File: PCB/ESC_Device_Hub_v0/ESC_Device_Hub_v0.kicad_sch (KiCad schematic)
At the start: 137 parts, among them J1 Conn_01x04, J10 Conn_01x06, J11 Conn_01x02, J12 Conn_01x02, J13 Conn_01x02, J14 Conn_01x02, J15 Conn_01x02, J16 Conn_01x02, J17 Conn_01x02, J18 Conn_01x02, J19 Conn_01x05, J2 Conn_01x04, J20 Conn_01x01, J21 Conn_01x01, J22 Conn_01x02, J3 Conn_01x04, J4 Conn_01x04, J5 Conn_01x04, J6 Conn_01x04, J7 Conn_01x06, J8 Conn_01x06, J9 Conn_01x06, SW1 SW_Push, SW2 SW_Push, SW3 SW_Coded_SH-7050, SW4 SW_DIP_x02, U1 ISO1042BQDWVQ1, U18 USB_Type-C, U2 MCP2562FD-H/MF, U3 IS25LP064D-JLLE, U4 STM32H563RGVx, U5 NJW1933F1-AT, U6 TLP293, U7 NJM2884U1-33, U8 XC8114AA01PR-G, U9 XC8114AA01PR-G, Y1 FC2012SN 32.768K-70NNA0KC0

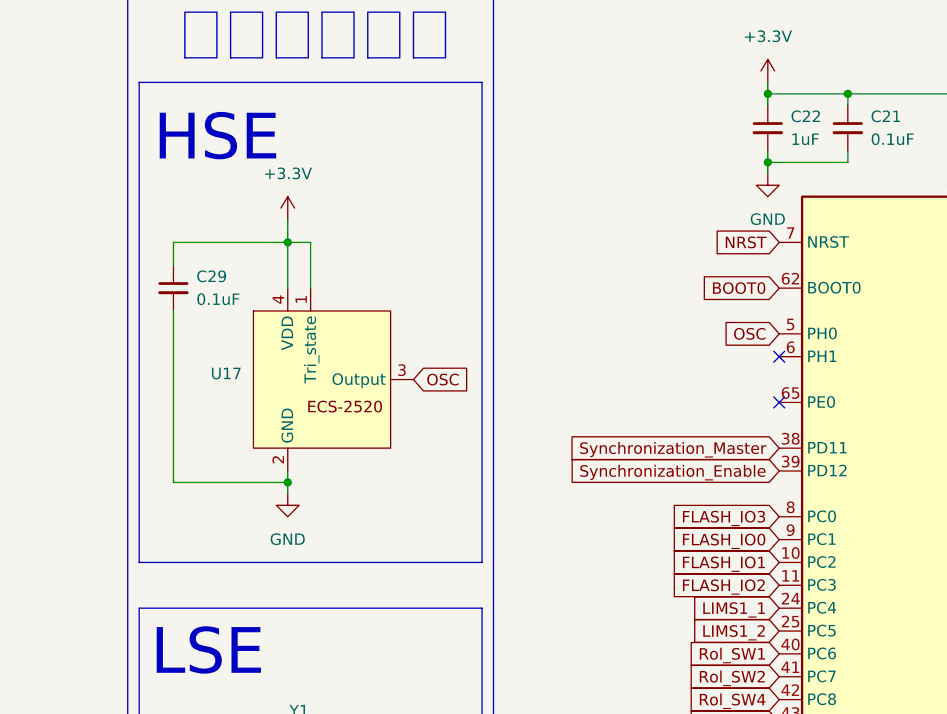
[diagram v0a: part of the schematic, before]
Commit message: CANFDのXHを縦にして発振器を変更
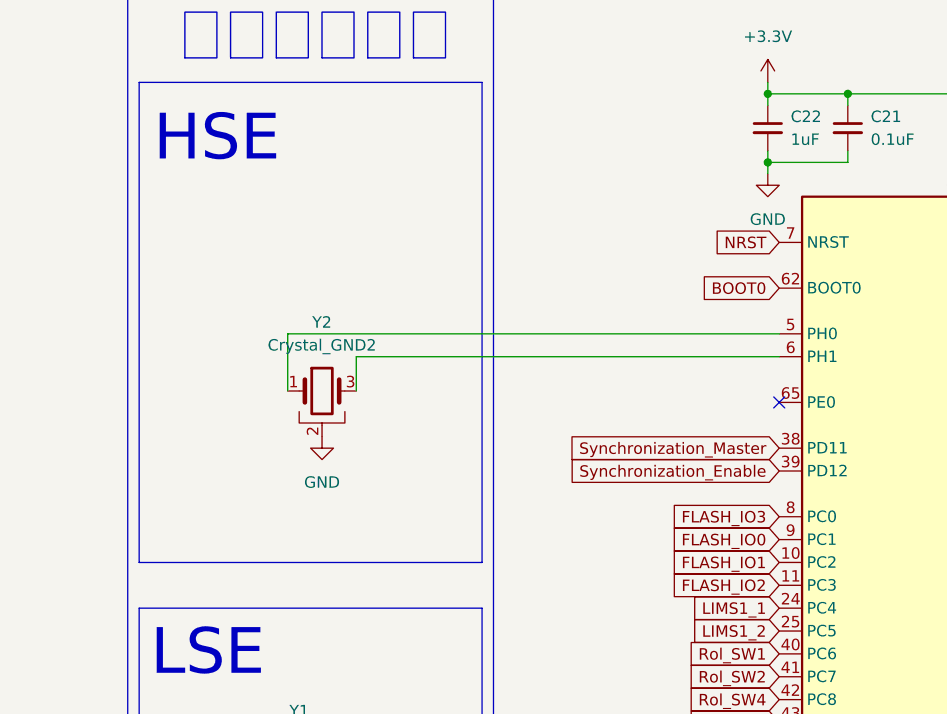
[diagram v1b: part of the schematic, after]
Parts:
- removed C29: 0.1uF, Capacitor_SMD:C_0402_1005Metric_Pad0.74x0.62mm_HandSolder, symbol Device:C_Small
- removed U17: (no value), My_Library:ECS-TXO-2520-33-500-AN-TR, symbol My_Library:ECS-TXO-2520-33-500-AN-TR
- added Y2: Crystal_GND2, Crystal:Resonator_SMD_Murata_CSTxExxV-3Pin_3.0x1.1mm, symbol Device:Crystal_GND2
- J1, J2: footprint Connector_JST:JST_XH_S4B-XH-A_1x04_P2.50mm_Horizontal -> Connector_JST:JST_XH_B4B-XH-A_1x04_P2.50mm_Vertical
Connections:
- net GND: now also Y2.2
- net at U4.6 (PH1): now also Y2.3
- net OSC: no longer names the net of U4.5 (PH0)
- net OSC: now also Y2.1
- no-connect marks 9 -> 8
